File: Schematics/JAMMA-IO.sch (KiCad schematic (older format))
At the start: 99 parts, among them CN1 B6P-VH, CN2 VGA-DSUB15, CN3 BS4PSHF1AA, U2 ADC0834

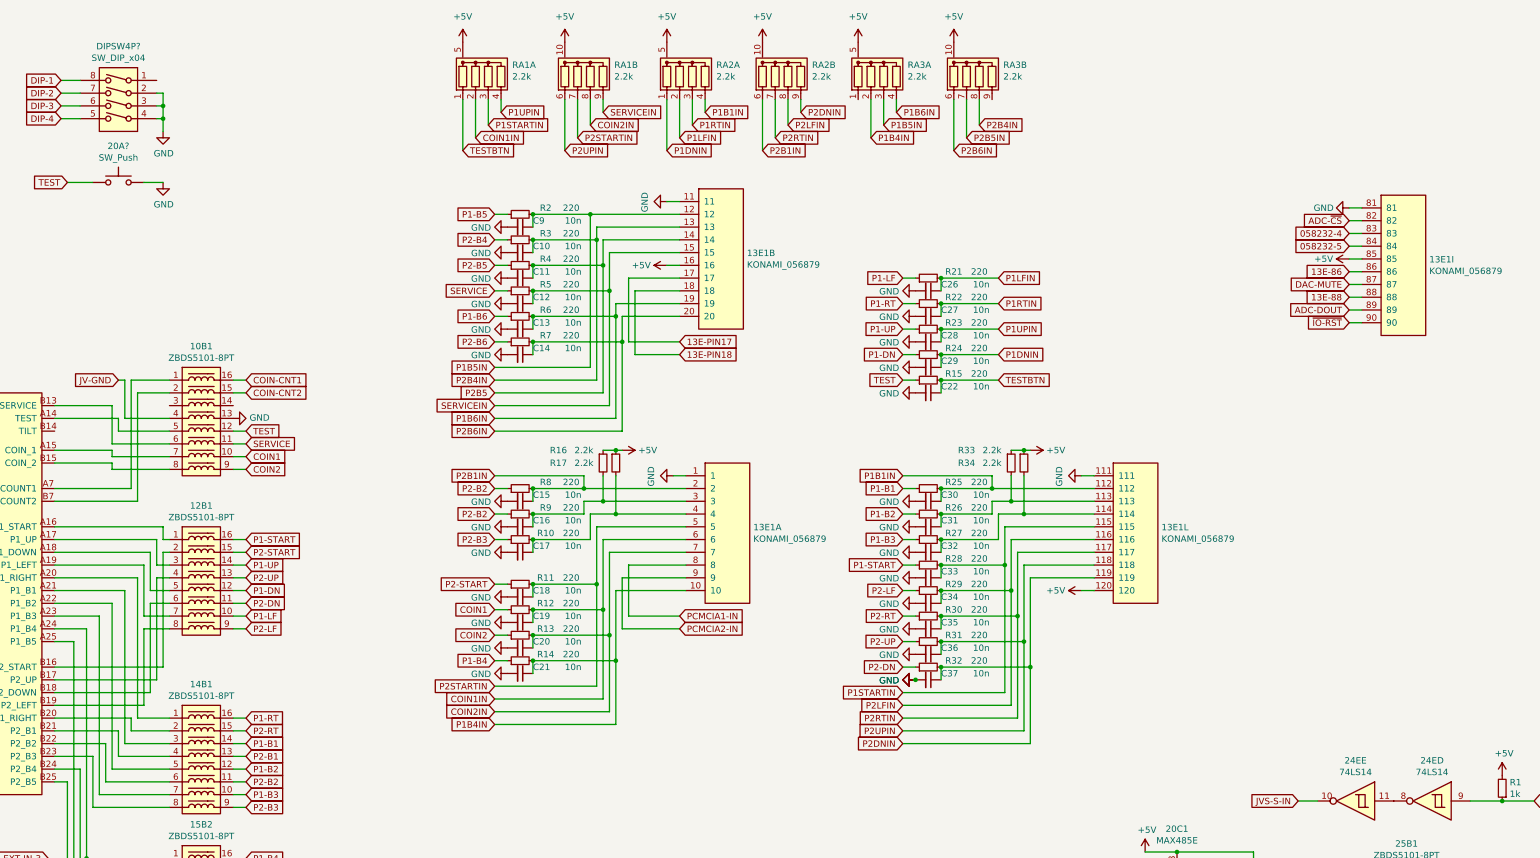
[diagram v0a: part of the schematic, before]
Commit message: Added GE675-PWB(A)
IO Board for Fisherman's Bait 3
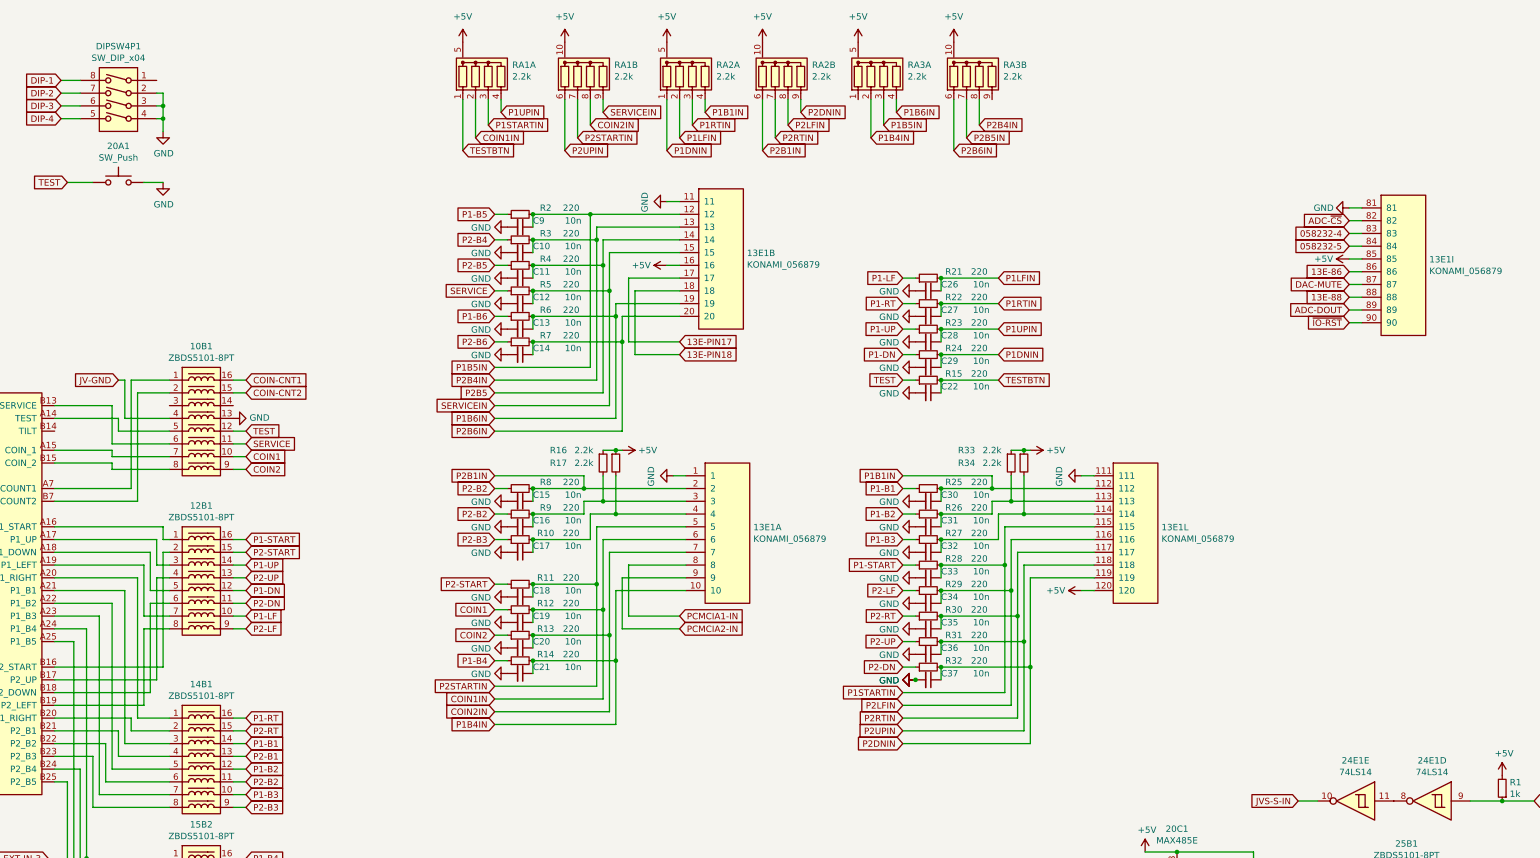
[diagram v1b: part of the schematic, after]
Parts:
- gave numbers to parts that had none: 2
- renumbered 24E to 24E1
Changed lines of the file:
@@
 $EndComp
 $Comp
-L 74xx:74LS14 24E
+L 74xx:74LS14 24E1
 U 4 1 627C8F3A
 P 14400 6850
-F 0 "24E" H 14400 7167 50  0000 C CNN
+F 0 "24E1" H 14400 7167 50  0000 C CNN
 F 1 "74LS14" H 14400 7076 50  0000 C CNN
 F 2 "Package_SO:SO-14_3.9x8.65mm_P1.27mm" H 14400 6850 50  0001 C CNN
@@
 $EndComp
 $Comp
-L 74xx:74LS14 24E
+L 74xx:74LS14 24E1
 U 5 1 62957C7E
 P 13800 6850
-F 0 "24E" H 13800 7167 50  0000 C CNN
+F 0 "24E1" H 13800 7167 50  0000 C CNN
 F 1 "74LS14" H 13800 7076 50  0000 C CNN
 F 2 "Package_SO:SO-14_3.9x8.65mm_P1.27mm" H 13800 6850 50  0001 C CNN
@@
 	13500 6850 13350 6850
 $Comp
-L power:GND #PWR?
+L power:GND #PWR0134
 U 1 1 647F650C
 P 4450 1600
-F 0 "#PWR?" H 4450 1350 50  0001 C CNN
+F 0 "#PWR0134" H 4450 1350 50  0001 C CNN
 F 1 "GND" H 4455 1427 50  0000 C CNN
 F 2 "" H 4450 1600 50  0001 C CNN
@@
 $EndComp
 $Comp
-L Switch:SW_DIP_x04 DIPSW4P?
+L Switch:SW_DIP_x04 DIPSW4P1
 U 1 1 647F6512
 P 4100 1400
-F 0 "DIPSW4P?" H 4100 1867 50  0000 C CNN
+F 0 "DIPSW4P1" H 4100 1867 50  0000 C CNN
 F 1 "SW_DIP_x04" H 4100 1776 50  0000 C CNN
 F 2 "Button_Switch_THT:SW_DIP_SPSTx04_Piano_10.8x11.72mm_W7.62mm_P2.54mm" H 4100 1400 50  0001 C CNN
@@
 	3800 1500 3650 1500
 $Comp
-L Switch:SW_Push 20A?
+L Switch:SW_Push 20A1
 U 1 1 647F6528
 P 4100 2000
-F 0 "20A?" H 4100 2285 50  0000 C CNN
+F 0 "20A1" H 4100 2285 50  0000 C CNN
 F 1 "SW_Push" H 4100 2194 50  0000 C CNN
 F 2 "Button_Switch_THT:SW_Tactile_SPST_Angled_PTS645Vx58-2LFS" H 4100 2200 50  0001 C CNN
@@
 $EndComp
 $Comp
-L power:GND #PWR?
+L power:GND #PWR0135
 U 1 1 647F652E
 P 4450 2000
-F 0 "#PWR?" H 4450 1750 50  0001 C CNN
+F 0 "#PWR0135" H 4450 1750 50  0001 C CNN
 F 1 "GND" H 4455 1827 50  0000 C CNN
 F 2 "" H 4450 2000 50  0001 C CNN

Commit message: Updated Schematics
PCMCIA is pinned out
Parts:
- added U?: KONAMI-058232, Arcade:KONAMI-SIP-14, symbol Arcade:KONAMI-058232
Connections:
- net +12V: now also U?.1 (COINC-FB)
- net +5V: now also U?.8 (VCC)
- net 058232-4: now also U?.4 (CC-IN2)
- net 058232-5: now also U?.5 (CC-IN1)
- net COIN-CNT1: now also U?.3 (CC-OUT1)
- net COIN-CNT2: now also U?.2 (CC-OUT2)
- net GND: now also U?.6 (GND), U?.7 (GND)
- new net 35J-11: U?.9 (WD-IN)
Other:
- moved on the sheet: 10B1, 12B1, 13E1A, 13E1B, 13E1I, 13E1L, 14B1, 15B2, 20A1, 2B1, 3B1, 4B1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

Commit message: Flash fixes, security cart done, most logic figured
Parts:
- added 12B2: ZBDS5101-8PT, Package_SO:SOIC-16_4.55x10.3mm_P1.27mm, symbol Filter:ZBDS5101-8PT
- added 26D1, 29D1: ZBF503D-00, Resistor_THT:R_Axial_DIN0204_L3.6mm_D1.6mm_P5.08mm_Horizontal, symbol Device:L_Core_Ferrite
- added 28E1, 29E1: 74LS07, Package_SO:SO-14_5.3x10.2mm_P1.27mm, symbol 74xx:74LS07
- added 2C1: EVQ-PC1, Button_Switch_THT:SW_Tactile_SPST_Angled_PTS645Vx58-2LFS, symbol Switch:SW_Push
- added CN5: B12PSHF1A, Connector_JST:JST_NH_B12P_SHD, symbol Connector_Generic:Conn_01x12
- gave numbers to parts that had none: 1
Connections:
- net ~IO-RST is gone; now on net ~RESET: 13E1.90
- net +5V: now also 26D1.1
- net GND: now also 29D1.1, 2C1.2
- net at U1.12 (~RESET_IN): now also 2C1.1
- net ~RESET: now reaches U1.13 (~WD_RESET)
- net 35J-11 renamed U71-43
- new net: 12B2.16, 28E1.2
- new net: 12B2.10, 29E1.12
- new net: 12B2.11, 28E1.8
- new net: 12B2.9, 29E1.2
- new net: 12B2.14, 28E1.4
- new net: 12B2.12, 28E1.6
- new net: 12B2.13, 28E1.10
- new net: 12B2.15, 28E1.12
- new net: 12B2.1, CN5.3 (Pin_3)
- new net: 12B2.2, CN5.4 (Pin_4)
- new net: 12B2.3, CN5.5 (Pin_5)
- new net: 12B2.4, CN5.6 (Pin_6)
- new net: 12B2.5, CN5.7 (Pin_7)
- new net: 12B2.6, CN5.8 (Pin_8)
- new net: 12B2.7, CN5.9 (Pin_9)
- new net: 12B2.8, CN5.10 (Pin_10)
- new net: 26D1.2, CN5.1 (Pin_1), CN5.2 (Pin_2)
- new net: 29D1.2, CN5.11 (Pin_11), CN5.12 (Pin_12)
- new net EXT-OUTPUT-0: 29E1.1
- new net EXT-OUTPUT-1: 29E1.13
- new net EXT-OUTPUT-2: 28E1.9
- new net EXT-OUTPUT-3: 28E1.5
- new net EXT-OUTPUT-4: 28E1.11
- new net EXT-OUTPUT-5: 28E1.3
- new net EXT-OUTPUT-6: 28E1.13
- new net EXT-OUTPUT-7: 28E1.1
- no-connect marks 0 -> 8
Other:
- note added: "External Outputs Header"
- note added: "Konami Watchdog"
- note added: "No connect"
- moved on the sheet: 15B1, 31A1, 33A1, 36A1, ANALOG-CN1, C23, C24, C25, C4, C5, C6, C7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

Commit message: 573 specific mostly mapped
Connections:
- net +5V: no longer 13E1.85
- net 058232-4: now also 13E1.84; no longer 13E1.83
- net 058232-5: now also 13E1.85; no longer 13E1.84
- net ADC-CLK: now also 13E1.83
- net 13E-86: no longer names the net of 13E1.86
- net 13E-88: no longer names the net of 13E1.88
- net 13E-PIN18 renamed RTC-FT
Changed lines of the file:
@@
 13E-PIN17
 Text GLabel 8100 4250 2    50   Input ~ 0
-13E-PIN18
+RTC-FT
 Wire Wire Line
 	8100 3650 7700 3650
@@
 ADC-~CS
 Text GLabel 11600 3350 0    50   Input ~ 0
+ADC-CLK
+Text GLabel 11600 3450 0    50   Input ~ 0
 058232-4
-Text GLabel 11600 3450 0    50   Input ~ 0
-058232-5
 $Comp
 L power:+5V #PWR?
 U 1 1 620037C6
-P 11600 3550
+P 12900 3150
 AR Path="/620037C6" Ref="#PWR?"  Part="1"
 AR Path="/63647603/620037C6" Ref="#PWR0105"  Part="1"
-F 0 "#PWR0105" H 11600 3400 50  0001 C CNN
-F 1 "+5V" V 11600 3750 50  0000 C CNN
-F 2 "" H 11600 3550 50  0001 C CNN
-F 3 "" H 11600 3550 50  0001 C CNN
-	1    11600 3550
+F 0 "#PWR0105" H 12900 3000 50  0001 C CNN
+F 1 "+5V" V 12900 3350 50  0000 C CNN
+F 2 "" H 12900 3150 50  0001 C CNN
+F 3 "" H 12900 3150 50  0001 C CNN
+	1    12900 3150
 	0    -1   -1   0
 $EndComp
@@
 	0    1    1    0
 $EndComp
-Text GLabel 11600 3650 0    50   Input ~ 0
-13E-86
 Text GLabel 11600 3750 0    50   Input ~ 0
 DAC-MUTE
-Text GLabel 11600 3850 0    50   Input ~ 0
-13E-88
 Text GLabel 11600 4050 0    50   Input ~ 0
 ~RESET
@@
 Wire Wire Line
 	13700 3750 13900 3750
+Text GLabel 11600 3550 0    50   Input ~ 0
+058232-5
 $EndSCHEMATC
